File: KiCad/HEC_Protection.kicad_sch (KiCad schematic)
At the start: 19 parts, among them U11 74LS00, U11 74LS32, U12 74LS04, U16 74LS32, U17 74LS74, U18 74LS138, U18 74LS74, U19 74LS30, U22 74LS02, U23 74LS74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

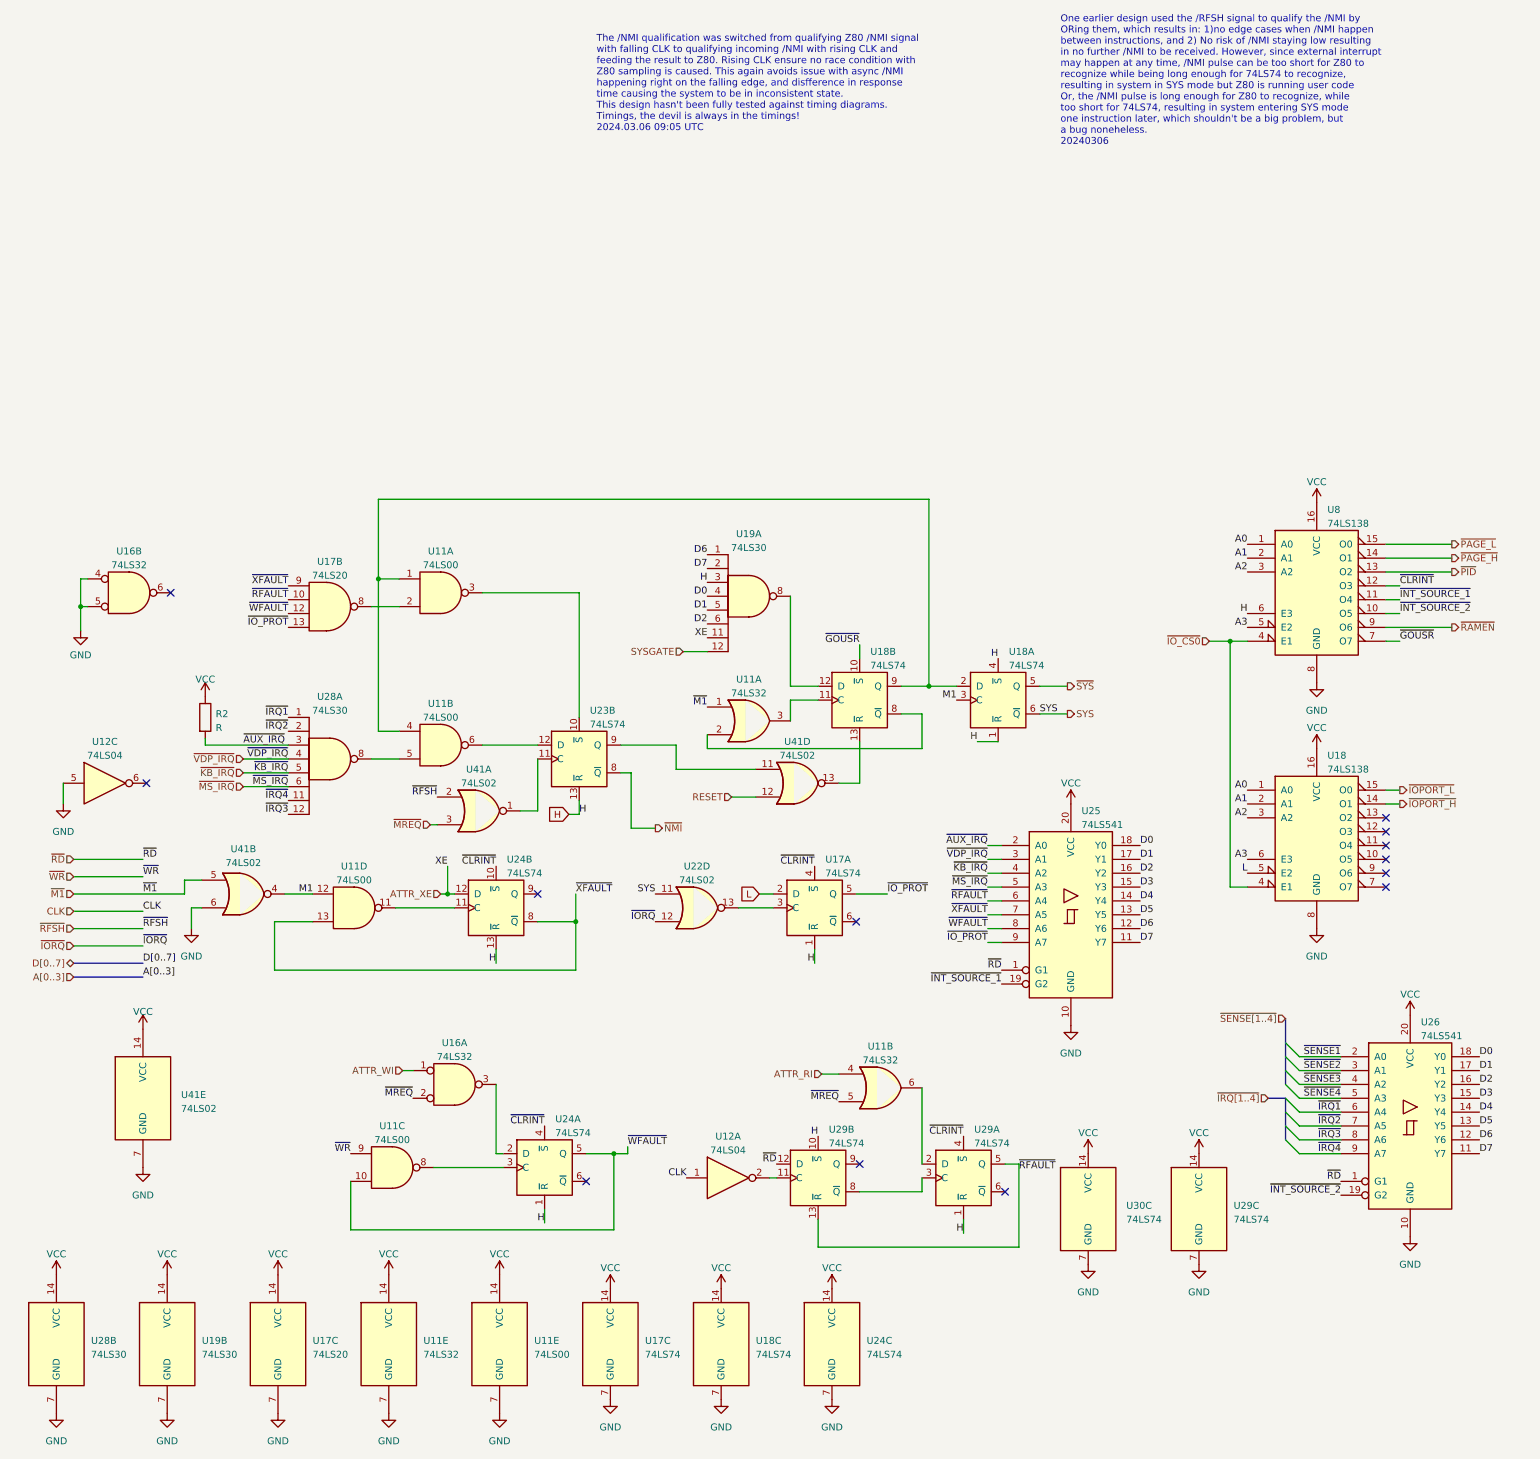
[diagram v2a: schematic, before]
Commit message: Protection Overhaul
Major change to the protection system. This change WILL break system software compatibility. Previously: bit 15: WP, 1=disable writing; bit 14: WI, 0=generate interrupt on write; bit 13: NX/XE 1/0=generate interrupt on M1 cycle; bit 12: RI 0=generate interrupt on read. New: bit 15: P, 0=not present, generate interrupt on MREQ access (any type of memory access except refresh); bit 14: WP, 0=read-only,1=read-write; bit 13: WI 0=generate interrupt on write; bit 12: XE 0=generate interrupt on M1.
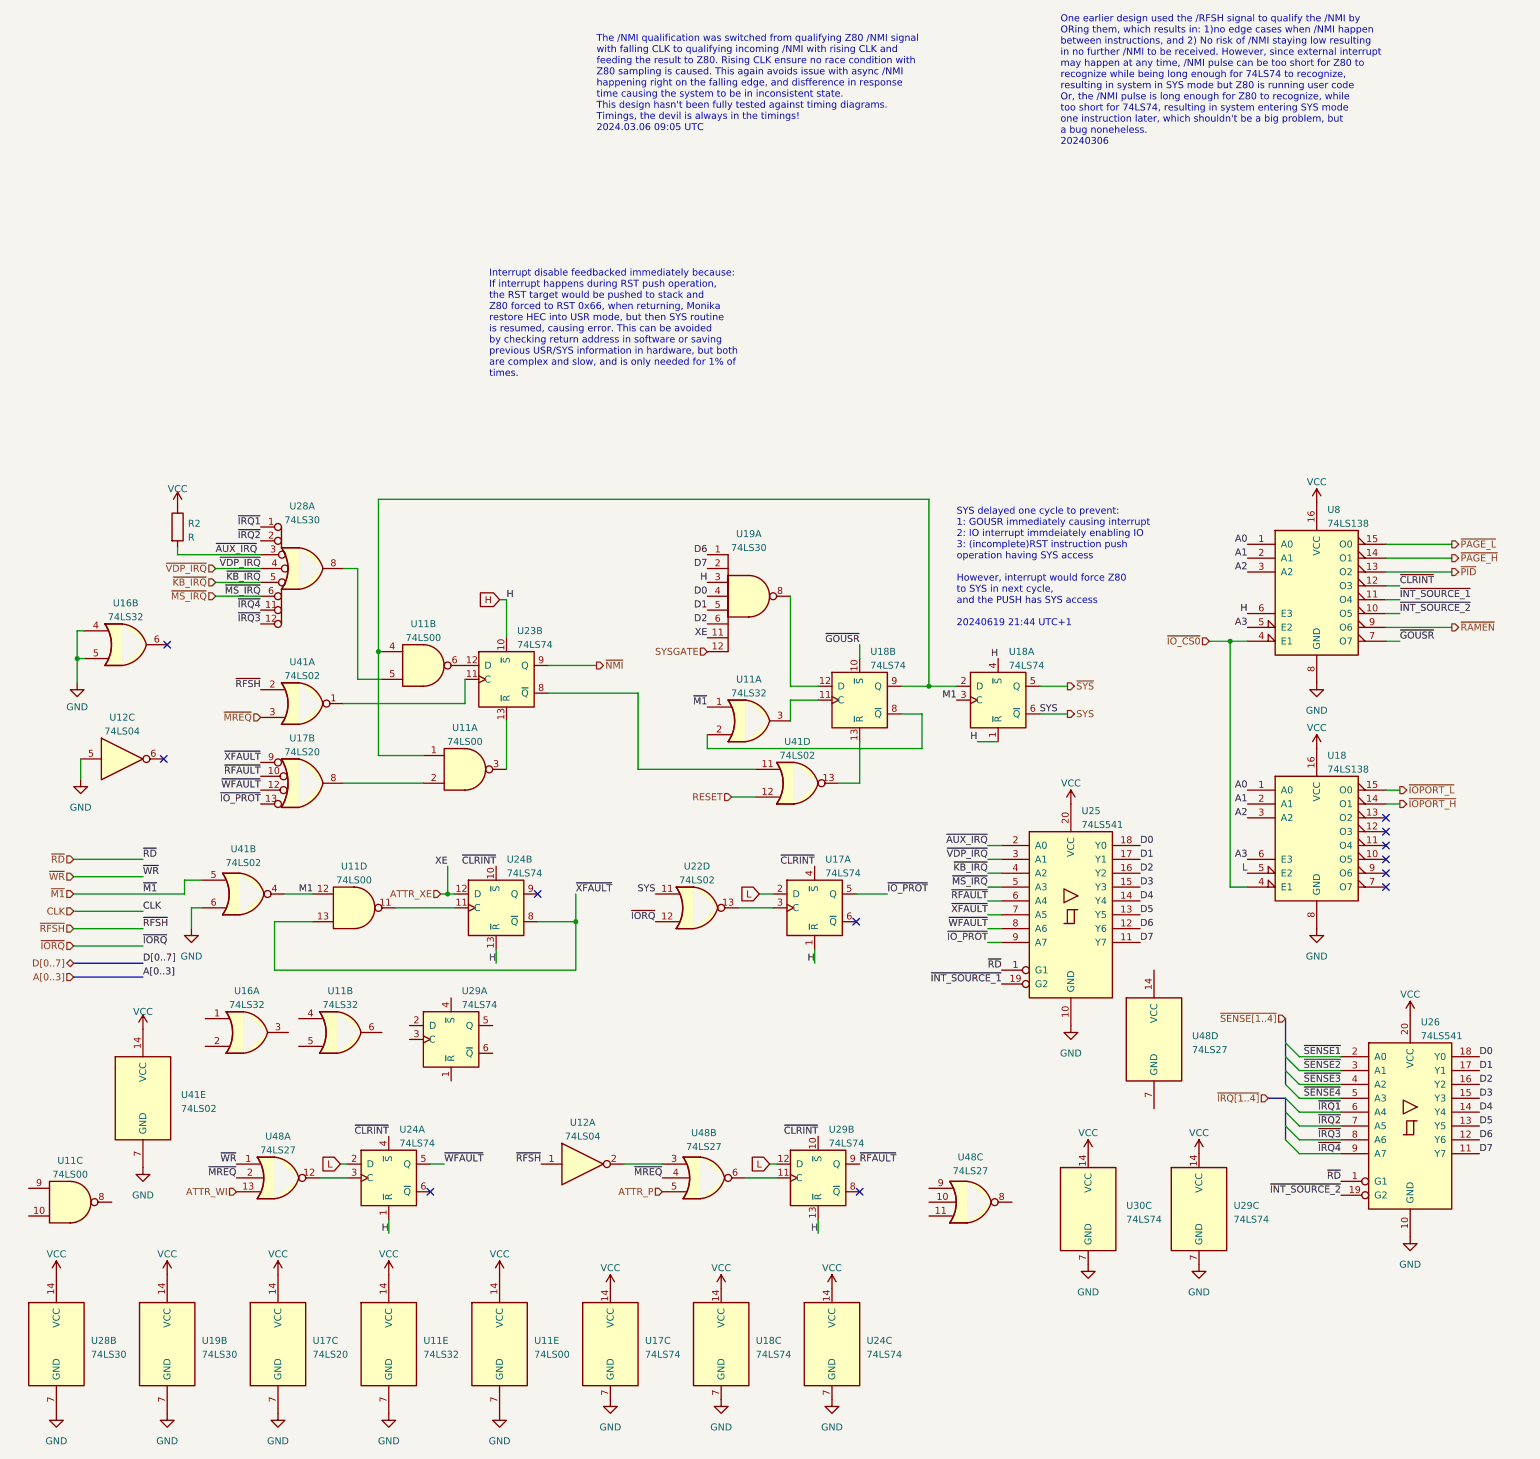
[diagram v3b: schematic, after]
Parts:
- added U48: 74LS27, symbol 74xx:74LS27
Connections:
- net ATTR_WI: now also U48.13; no longer U16.1
- net CLK: no longer U12.1
- net H: now also U23.10 (~{S}), U29.13 (~{R}); no longer U23.13 (~{R}), U29.1 (~{R}), U29.10 (~{S})
- net L: now also U24.2 (D), U29.12 (D)
- net ~{CLRINT}: now also U29.10 (~{S}); no longer U29.4 (~{S})
- net ~{MREQ}: now also U48.2, U48.4; no longer U11.5, U16.2
- net ~{NMI}: now also U23.9 (Q); no longer U23.8 (~{Q})
- net ~{RD}: no longer U29.12 (D)
- net ~{RFAULT}: now also U29.9 (Q); no longer U29.13 (~{R}), U29.5 (Q)
- net ~{RFSH}: now also U12.1
- net ~{WFAULT}: no longer U11.10
- net ~{WR}: now also U48.1; no longer U11.9
- net at U11.6: no longer U29.2 (D)
- net at U29.11 (C): now also U48.6; no longer U12.2
- net at U29.8 (~{Q}): no longer U29.3 (C)
- net at U11.8: no longer U24.3 (C)
- net at U41.11: now also U23.8 (~{Q}); no longer U23.9 (Q)
- net at U11.3: now also U23.13 (~{R}); no longer U23.10 (~{S})
- net at U16.3: no longer U24.2 (D)
- net ATTR_RI: no longer names the net of U11.4
- new net: U12.2, U48.3
- new net: U24.3 (C), U48.12
- new net ATTR_P: U48.5
- no-connect marks 13 -> 12
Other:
- note added: "Interrupt disable feedbacked immediately because: If interrupt happens during RST push operation, the RST target would be pushed to stack and Z80 forced to RST 0x66, when returning, Monika restore HEC into USR mode, but then SYS routine is resumed, causing error. This can be avoided by checking return address in software or saving previous USR/SYS information in hardware, but both are complex and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"
- note added: "SYS delayed one cycle to prevent: 1: GOUSR immediately causing interrupt 2: IO interrupt immdeiately enabling IO 3: (incomplete)RST instruction push operation having SYS access However, interrupt would force Z80 to SYS in next cycle, and the PUSH has SYS access 20240619 21:44 UTC+1"
- moved on the sheet: R2, U11A, U11B, U11C, U12A, U12C, U23B, U24A, U29A, U41A

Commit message: Finish protection overhaul
Disable ram chip select when page is marked as not present, change write protect to 1 as write enabled, 0 as disabled. Change XE interrupt timings.
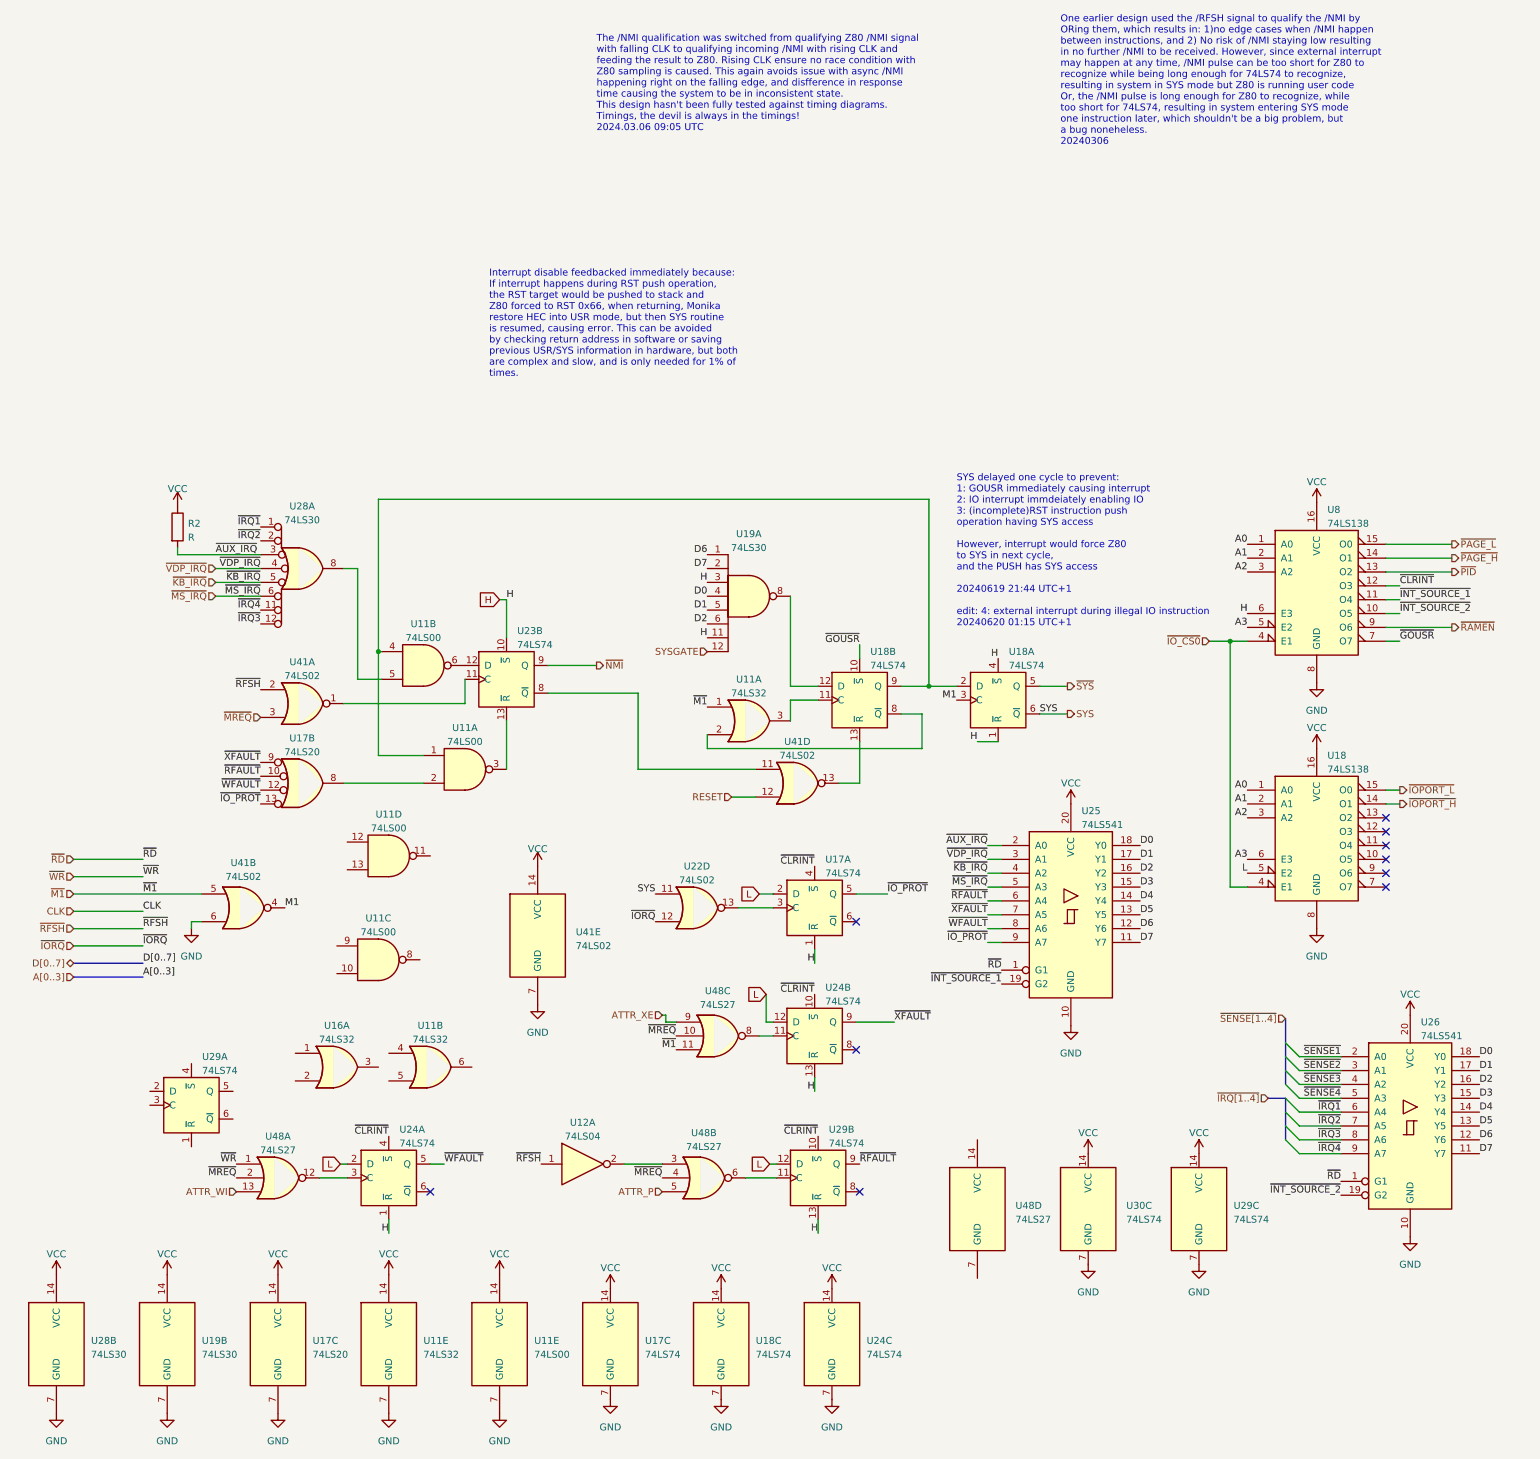
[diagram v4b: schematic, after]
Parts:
- removed unit 3 of U12
- removed unit 2 of U16
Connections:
- net ATTR_XE: now also U48.9; no longer U19.11, U24.12 (D)
- net H: now also U19.11
- net L: now also U24.12 (D)
- net M1: no longer U11.12
- net ~{M1}: now also U48.11
- net ~{MREQ}: now also U48.10
- net ~{XFAULT}: now also U24.9 (Q); no longer U11.13, U24.8 (~{Q})
- net at U24.11 (C): now also U48.8; no longer U11.11
- no-connect marks 12 -> 10
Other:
- note added: "SYS delayed one cycle to prevent: 1: GOUSR immediately causing interrupt 2: IO interrupt immdeiately enabling IO 3: (incomplete)RST instruction push operation having SYS access However, interrupt would force Z80 to SYS in next cycle, and the PUSH has SYS access 20240619 21:44 UTC+1 edit: 4: external interrupt during illegal IO instruction 20240620 01:15 UTC+1"
- note removed: "SYS delayed one cycle to prevent: 1: GOUSR immediately causing interrupt 2: IO interrupt immdeiately enabling IO 3: (incomplete)RST instruction push operation having SYS access However, interrupt would force Z80 to SYS in next cycle, and the PUSH has SYS access 20240619 21:44 UTC+1"
- moved on the sheet: U11B, U11C, U11D, U16A, U24B, U29A, U41B, U41E, U48C, U48D
